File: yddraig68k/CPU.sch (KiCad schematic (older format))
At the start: 30 parts, among them J301 Conn_01x02, SW301 SW_DPST, U301 74LS06, U302 NE555P, U303 68000D, U304 74LS32, U305 SST39SF040, U306 SST39SF040, U307 AS6C4008-55PCN, U308 AS6C4008-55PCN

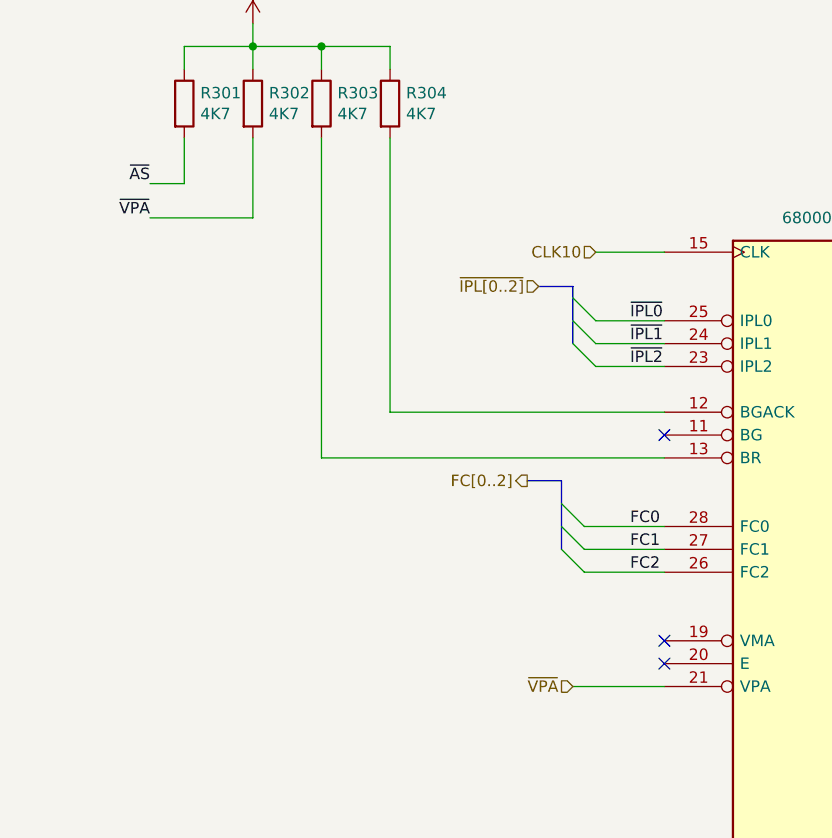
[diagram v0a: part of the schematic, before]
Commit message: Changed schematic to more match proteus version
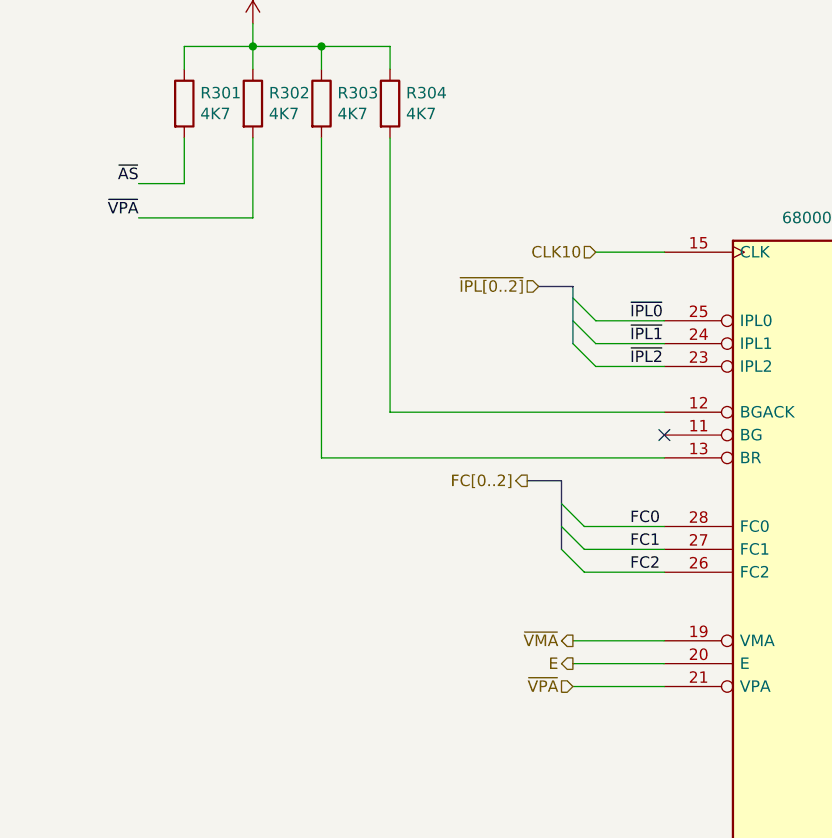
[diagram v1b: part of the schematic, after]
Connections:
- net ~VMA: now reaches U303.19 (VMA)
- net E: now reaches U303.20 (E)
- no-connect marks 6 -> 4
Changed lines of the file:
@@
 	1    0    0    -1
 $EndComp
-Text Label 1550 1550 2    50   ~ 0
+Text Label 1500 1550 2    50   ~ 0
 ~AS
 Text HLabel 3250 2000 0    50   Input ~ 0
@@
 Wire Wire Line
 	2300 2750 2300 1350
-Text Label 1550 1700 2    50   ~ 0
+Text Label 1500 1700 2    50   ~ 0
 ~VPA
 Wire Wire Line
-	1550 1550 1700 1550
-Wire Wire Line
 	1700 1550 1700 1350
-Wire Wire Line
-	1550 1700 2000 1700
 Wire Wire Line
 	2000 1700 2000 1350
@@
 	1    0    0    -1
 $EndComp
-NoConn ~ 3800 3550
-NoConn ~ 3800 3650
+Text HLabel 3400 3550 0    50   Output ~ 0
+~VMA
+Text HLabel 3400 3650 0    50   Output ~ 0
+E
+Wire Wire Line
+	3800 3650 3400 3650
+Wire Wire Line
+	3400 3550 3800 3550
+Wire Wire Line
+	1700 1550 1500 1550
+Wire Wire Line
+	1500 1700 2000 1700
 Wire Bus Line
 	3400 2000 3400 2250

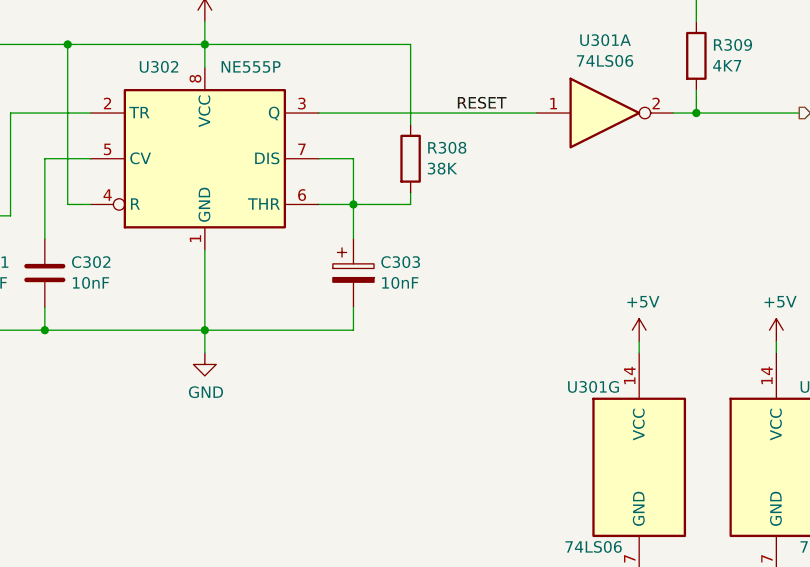
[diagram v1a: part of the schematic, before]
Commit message: More progress on VGA card design
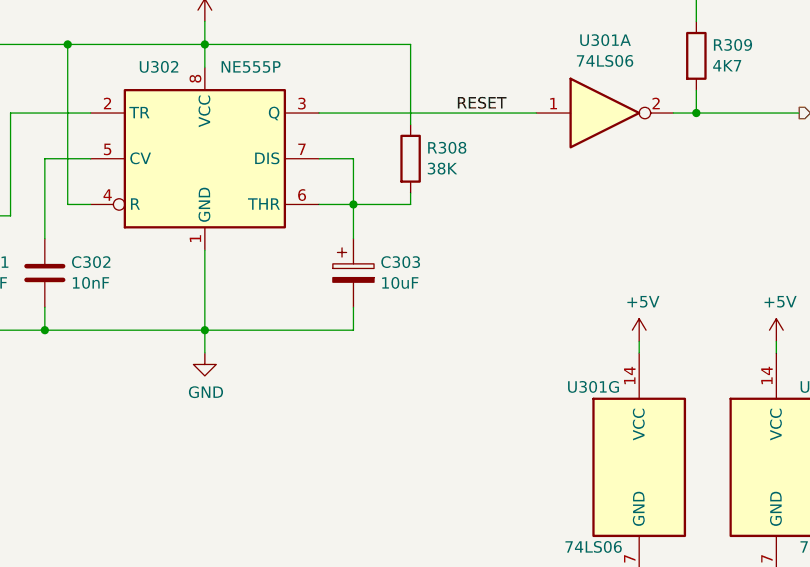
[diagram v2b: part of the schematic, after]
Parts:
- C302: footprint Capacitor_THT:CP_Radial_D5.0mm_P2.50mm -> Capacitor_THT:C_Disc_D3.8mm_W2.6mm_P2.50mm
- C303: value 10nF -> 10uF
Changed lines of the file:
@@
 P 4950 9400
 F 0 "C303" H 5068 9446 50  0000 L CNN
-F 1 "10nF" H 5068 9355 50  0000 L CNN
+F 1 "10uF" H 5068 9355 50  0000 L CNN
 F 2 "Capacitor_THT:CP_Radial_D5.0mm_P2.50mm" H 4988 9250 50  0001 C CNN
 F 3 "~" H 4950 9400 50  0001 C CNN
@@
 F 0 "C302" H 3715 9446 50  0000 L CNN
 F 1 "10nF" H 3715 9355 50  0000 L CNN
-F 2 "Capacitor_THT:CP_Radial_D5.0mm_P2.50mm" H 3638 9250 50  0001 C CNN
+F 2 "Capacitor_THT:C_Disc_D3.8mm_W2.6mm_P2.50mm" H 3638 9250 50  0001 C CNN
 F 3 "~" H 3600 9400 50  0001 C CNN
 	1    3600 9400

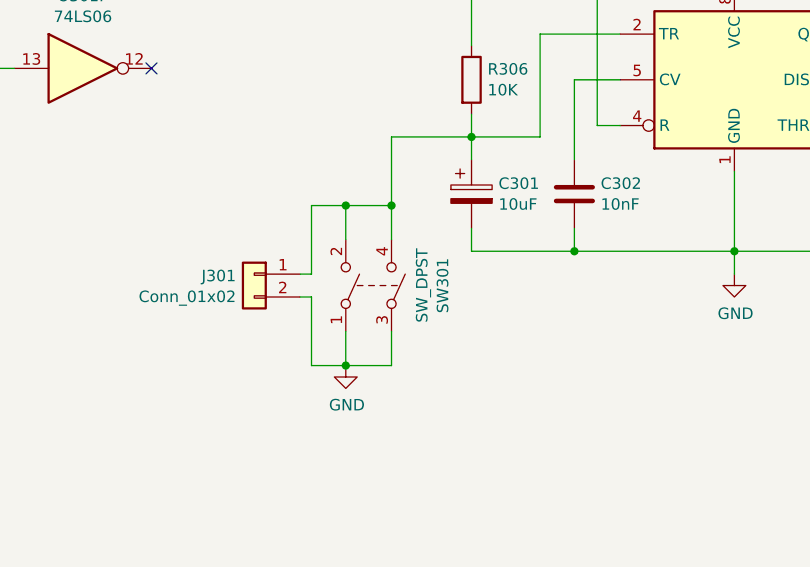
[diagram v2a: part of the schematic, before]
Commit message: Fix for POWER and RESET switches
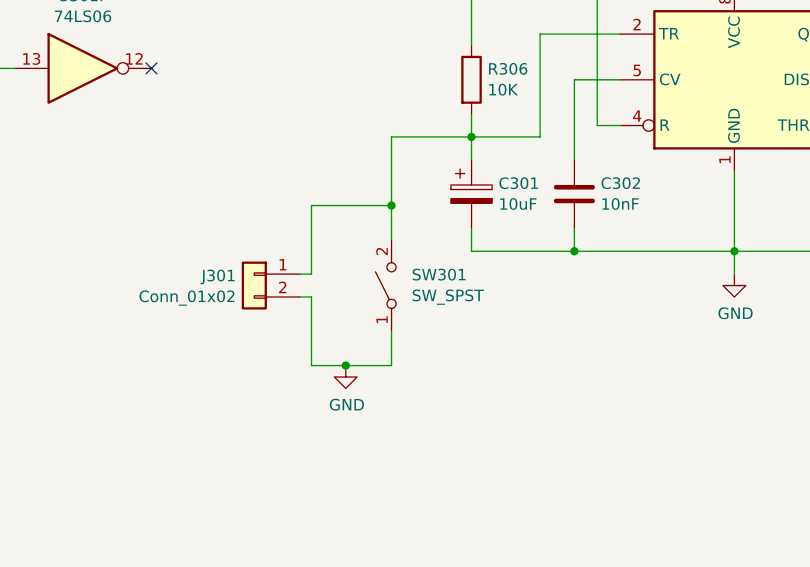
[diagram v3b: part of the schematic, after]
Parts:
- removed SW301: SW_DPST, Button_Switch_THT:SW_TH_Tactile_Omron_B3F-10xx, symbol Switch:SW_DPST
- added SW301: SW_SPST, Button_Switch_THT:SW_PUSH_6mm_H4.3mm, symbol Switch:SW_SPST
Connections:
- net GND: now also SW301.1 (A)
- net at C301.1, J301.1 (Pin_1), R306.2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: now also SW301.2 (B)
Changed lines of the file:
@@
-$EndComp
-$Comp
-L Switch:SW_DPST SW?
-U 1 1 609F7730
-P 2700 9800
-AR Path="/6058AC66/609F7730" Ref="SW?"  Part="1"
-AR Path="/606E9E62/609F7730" Ref="SW301"  Part="1"
-F 0 "SW301" H 2700 10125 50  0000 C CNN
-F 1 "SW_DPST" H 2700 10034 50  0000 C CNN
-F 2 "Button_Switch_THT:SW_TH_Tactile_Omron_B3F-10xx" H 2700 9800 50  0001 C CNN
-F 3 "~" H 2700 9800 50  0001 C CNN
-	1    2700 9800
-	0    1    -1   0
 $EndComp
 $Comp
@@
 Wire Wire Line
 	2800 9600 2800 9450
-Wire Wire Line
-	2800 9450 2600 9450
 $Comp
 L Device:R R306
@@
 $EndComp
 Wire Wire Line
-	2600 10000 2600 10150
-Wire Wire Line
-	2600 9450 2600 9600
-Wire Wire Line
 	2400 9750 2450 9750
 Wire Wire Line
 	2450 9750 2450 9450
-Wire Wire Line
-	2450 9450 2600 9450
-Connection ~ 2600 9450
 Wire Wire Line
 	2400 9850 2450 9850
@@
 Wire Wire Line
 	1500 1700 2000 1700
+$Comp
+L Switch:SW_SPST SW?
+U 1 1 61295AFD
+P 2800 9800
+AR Path="/6058AC66/61295AFD" Ref="SW?"  Part="1"
+AR Path="/606E9E62/61295AFD" Ref="SW301"  Part="1"
+F 0 "SW301" V 2846 9712 50  0000 R CNN
+F 1 "SW_SPST" V 2755 9712 50  0000 R CNN
+F 2 "Button_Switch_THT:SW_PUSH_6mm_H4.3mm" H 2800 9800 50  0001 C CNN
+F 3 "~" H 2800 9800 50  0001 C CNN
+	1    2800 9800
+	0    -1   -1   0
+$EndComp
 Wire Bus Line
 	3400 2000 3400 2250
@@
 Wire Bus Line
 	6350 1700 6350 3950
+Wire Wire Line
+	2450 9450 2800 9450
 $EndSCHEMATC

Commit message: Updated labeling on Y ddraig board
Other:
- note added: "EVEN\n"
- note added: "ODD"
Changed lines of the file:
@@
 	0    -1   -1   0
 $EndComp
+Wire Wire Line
+	2450 9450 2800 9450
 Wire Bus Line
 	3400 2000 3400 2250
@@
 Wire Bus Line
 	6350 1700 6350 3950
-Wire Wire Line
-	2450 9450 2800 9450
+Text Notes 12250 2750 0    150  ~ 0
+ODD
+Text Notes 12700 7450 0    150  ~ 0
+EVEN\n
 $EndSCHEMATC
